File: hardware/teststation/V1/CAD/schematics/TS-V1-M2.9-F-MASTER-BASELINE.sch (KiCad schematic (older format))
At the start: 0 parts

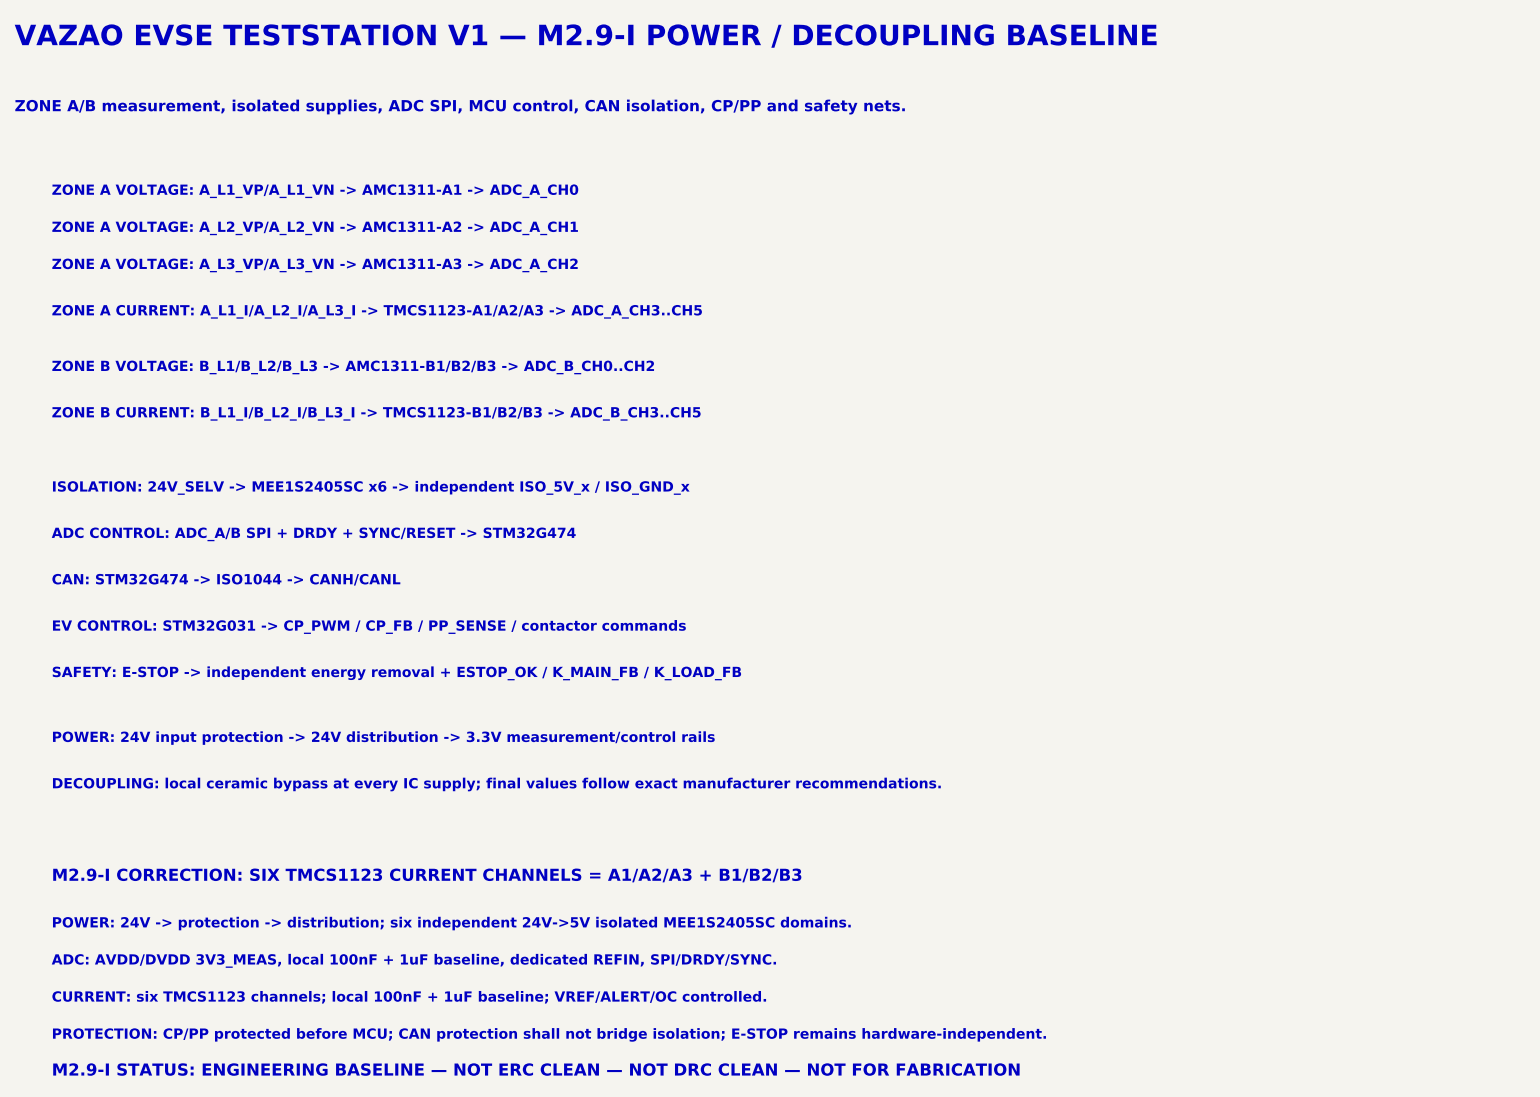
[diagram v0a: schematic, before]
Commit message: M2.9-L build real legacy component and net connectivity source
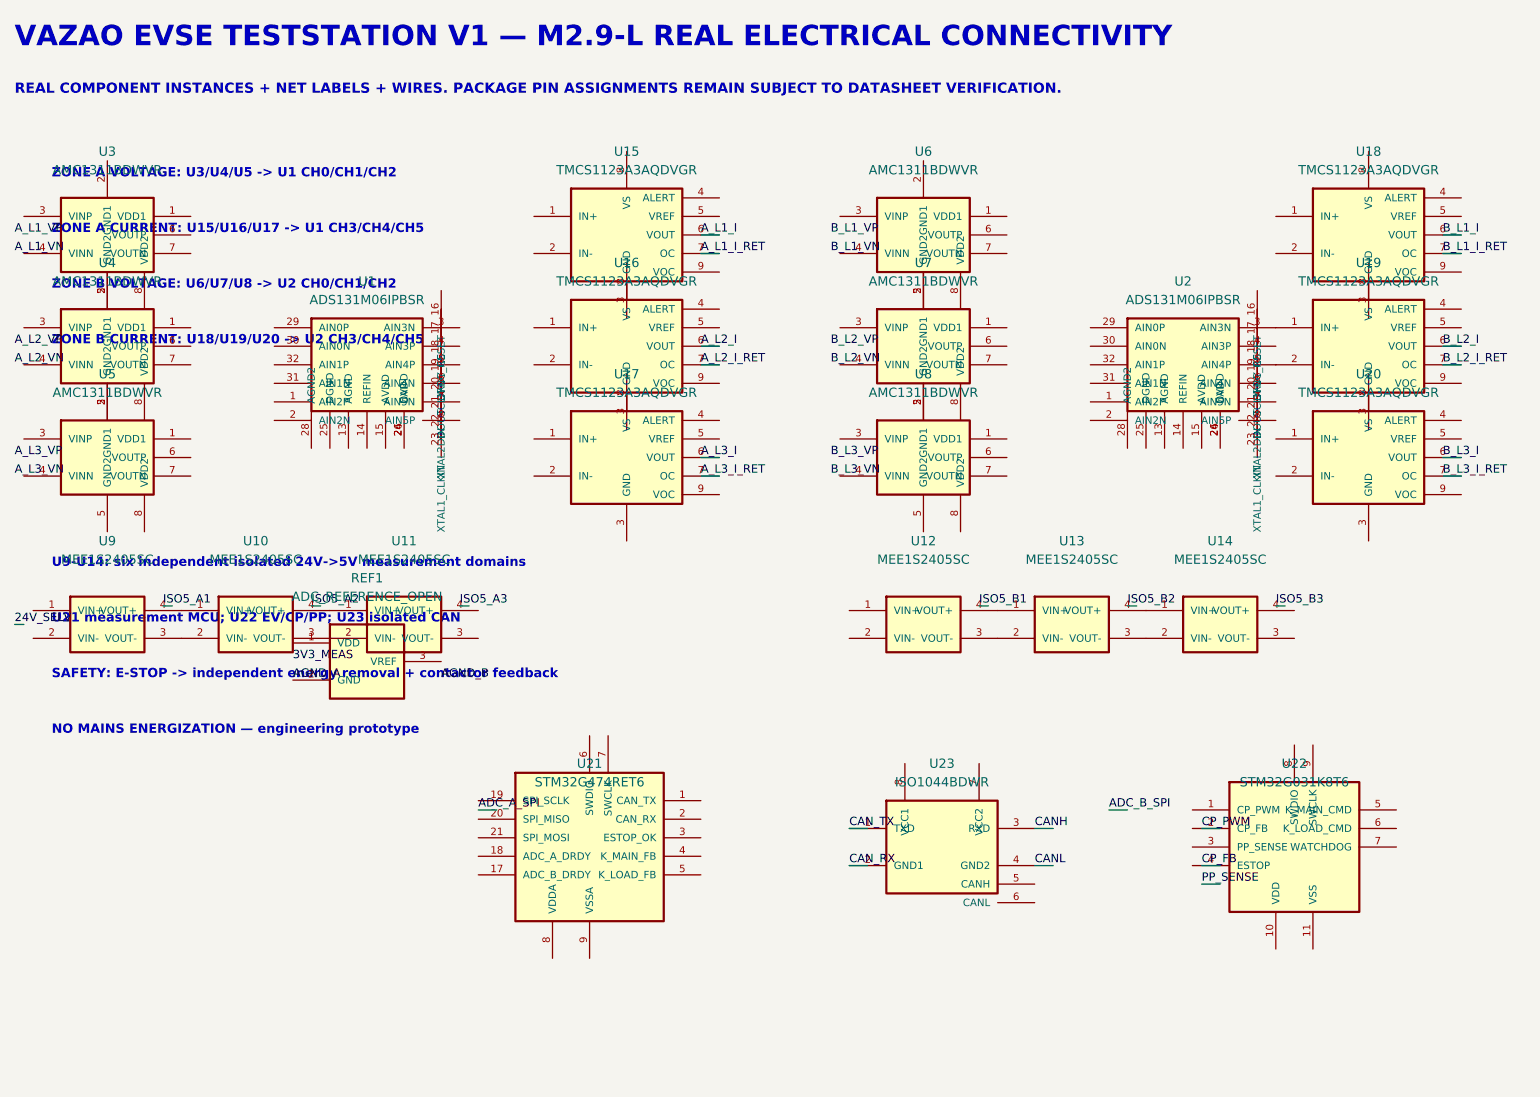
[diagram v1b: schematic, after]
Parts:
- added REF1: ADC_REFERENCE_OPEN, symbol TS-V1-M2.9-F-MASTER-BASELINE-cache:REF_ADC
- added U1, U2: ADS131M06IPBSR, symbol TS-V1-M2.9-F-MASTER-BASELINE-cache:ADS131M06IPBSR
- added U10, U11, U12, U13, U14, U9: MEE1S2405SC, symbol TS-V1-M2.9-F-MASTER-BASELINE-cache:MEE1S2405SC
- added U15, U16, U17, U18, U19, U20: TMCS1123A3AQDVGR, symbol TS-V1-M2.9-F-MASTER-BASELINE-cache:TMCS1123A3AQDVGR
- added U21: STM32G474RET6, symbol TS-V1-M2.9-F-MASTER-BASELINE-cache:STM32G474RET6
- added U22: STM32G031K8T6, symbol TS-V1-M2.9-F-MASTER-BASELINE-cache:STM32G031K8T6
- added U23: ISO1044BDWR, symbol TS-V1-M2.9-F-MASTER-BASELINE-cache:ISO1044BDWR
- added U3, U4, U5, U6, U7, U8: AMC1311BDWVR, symbol TS-V1-M2.9-F-MASTER-BASELINE-cache:AMC1311BDWVR
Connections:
- net labels added: 24V_SELV, 3V3_MEAS, ADC_A_SPI, ADC_B_SPI, AGND_A, AGND_B, A_L1_I, A_L1_I_RET, A_L1_VN, A_L1_VP, A_L2_I, A_L2_I_RET, A_L2_VN, A_L2_VP, A_L3_I, A_L3_I_RET, A_L3_VN, A_L3_VP, B_L1_I, B_L1_I_RET, B_L1_VN, B_L1_VP, B_L2_I, B_L2_I_RET, B_L2_VN, B_L2_VP, B_L3_I, B_L3_I_RET, B_L3_VN, B_L3_VP, CANH, CANL, CAN_RX, CAN_TX, CP_FB, CP_PWM, ISO5_A1, ISO5_A2, ISO5_A3, ISO5_B1, ISO5_B2, ISO5_B3, PP_SENSE
- wire segments 0 -> 40
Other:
- note added: "NO MAINS ENERGIZATION — engineering prototype"
- note added: "REAL COMPONENT INSTANCES + NET LABELS + WIRES. PACKAGE PIN ASSIGNMENTS REMAIN SUBJECT TO DATASHEET VERIFICATION."
- note added: "SAFETY: E-STOP -> independent energy removal + contactor feedback"
- note added: "U21 measurement MCU; U22 EV/CP/PP; U23 isolated CAN"
- note added: "U9-U14: six independent isolated 24V->5V measurement domains"
- note added: "VAZAO EVSE TESTSTATION V1 — M2.9-L REAL ELECTRICAL CONNECTIVITY"
- note added: "ZONE A CURRENT: U15/U16/U17 -> U1 CH3/CH4/CH5"
- note added: "ZONE A VOLTAGE: U3/U4/U5 -> U1 CH0/CH1/CH2"
- note added: "ZONE B CURRENT: U18/U19/U20 -> U2 CH3/CH4/CH5"
- note added: "ZONE B VOLTAGE: U6/U7/U8 -> U2 CH0/CH1/CH2"
- note removed: "ADC CONTROL: ADC_A/B SPI + DRDY + SYNC/RESET -> STM32G474"
- note removed: "ADC: AVDD/DVDD 3V3_MEAS, local 100nF + 1uF baseline, dedicated REFIN, SPI/DRDY/SYNC."
- note removed: "CAN: STM32G474 -> ISO1044 -> CANH/CANL"
- note removed: "CURRENT: six TMCS1123 channels; local 100nF + 1uF baseline; VREF/ALERT/OC controlled."
- note removed: "DECOUPLING: local ceramic bypass at every IC supply; final values follow exact manufacturer recommendations."
- note removed: "EV CONTROL: STM32G031 -> CP_PWM / CP_FB / PP_SENSE / contactor commands"
- note removed: "ISOLATION: 24V_SELV -> MEE1S2405SC x6 -> independent ISO_5V_x / ISO_GND_x"
- note removed: "M2.9-I CORRECTION: SIX TMCS1123 CURRENT CHANNELS = A1/A2/A3 + B1/B2/B3"
- note removed: "M2.9-I STATUS: ENGINEERING BASELINE — NOT ERC CLEAN — NOT DRC CLEAN — NOT FOR FABRICATION"
- note removed: "POWER: 24V -> protection -> distribution; six independent 24V->5V isolated MEE1S2405SC domains."
- note removed: "POWER: 24V input protection -> 24V distribution -> 3.3V measurement/control rails"
- note removed: "PROTECTION: CP/PP protected before MCU; CAN protection shall not bridge isolation; E-STOP remains hardware-independent."
- note removed: "SAFETY: E-STOP -> independent energy removal + ESTOP_OK / K_MAIN_FB / K_LOAD_FB"
- note removed: "VAZAO EVSE TESTSTATION V1 — M2.9-I POWER / DECOUPLING BASELINE"
- note removed: "ZONE A CURRENT: A_L1_I/A_L2_I/A_L3_I -> TMCS1123-A1/A2/A3 -> ADC_A_CH3..CH5"
- note removed: "ZONE A VOLTAGE: A_L1_VP/A_L1_VN -> AMC1311-A1 -> ADC_A_CH0"
- note removed: "ZONE A VOLTAGE: A_L2_VP/A_L2_VN -> AMC1311-A2 -> ADC_A_CH1"
- note removed: "ZONE A VOLTAGE: A_L3_VP/A_L3_VN -> AMC1311-A3 -> ADC_A_CH2"
- note removed: "ZONE A/B measurement, isolated supplies, ADC SPI, MCU control, CAN isolation, CP/PP and safety nets."
- note removed: "ZONE B CURRENT: B_L1_I/B_L2_I/B_L3_I -> TMCS1123-B1/B2/B3 -> ADC_B_CH3..CH5"
- note removed: "ZONE B VOLTAGE: B_L1/B_L2/B_L3 -> AMC1311-B1/B2/B3 -> ADC_B_CH0..CH2"
